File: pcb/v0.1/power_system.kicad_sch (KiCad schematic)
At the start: 6 parts, among them J12 USB_C_Receptacle_USB2.0

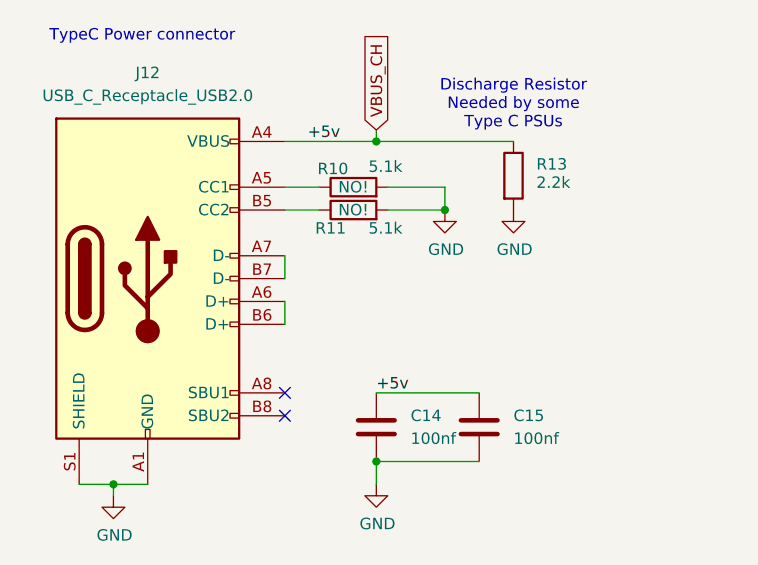
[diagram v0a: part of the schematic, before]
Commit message: More work on the sound system
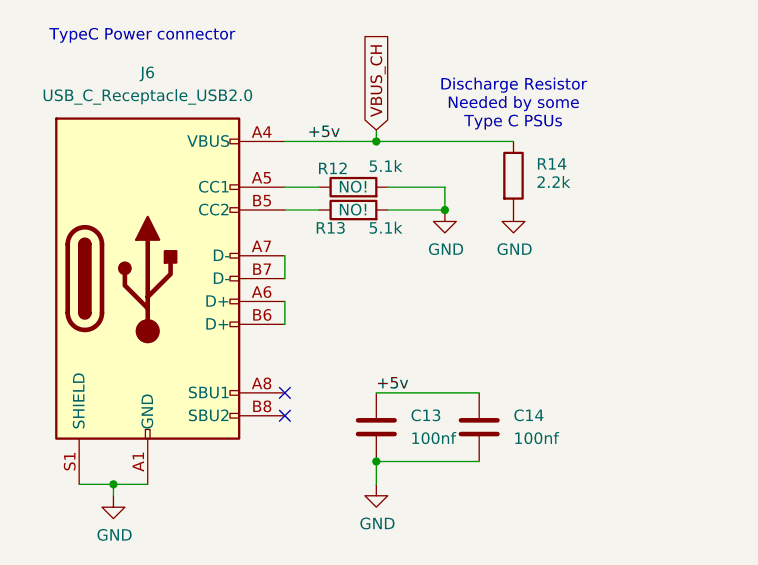
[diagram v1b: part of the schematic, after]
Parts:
- renumbered C14 to C13, C15 to C14, J12 to J6, R10 to R12, R11 to R13, R13 to R14
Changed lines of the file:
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@@
 		(dnp no)
 		(fields_autoplaced yes)
-		(property "Reference" "C15"
+		(property "Reference" "C14"
 			(at 106.68 87.63 0)
 			(show_name no)
@@
 			(project "mainboard"
 				(path "/5b8aa782-5c3d-43e7-a869-3bd000015f52/6125d0a9-a152-4232-a300-1c14841893d5"
-					(reference "C15")
+					(reference "C14")
 					(unit 1)
 				)
@@
 		(in_pos_files yes)
 		(dnp no)
-		(property "Reference" "#PWR020"
+		(property "Reference" "#PWR030"
 			(at 62.23 102.87 0)
 			(hide yes)
@@
 			(project "mainboard"
 				(path "/5b8aa782-5c3d-43e7-a869-3bd000015f52/6125d0a9-a152-4232-a300-1c14841893d5"
-					(reference "#PWR020")
+					(reference "#PWR030")
 					(unit 1)
 				)
@@
 		(in_pos_files yes)
 		(dnp no)
-		(property "Reference" "R11"
+		(property "Reference" "R13"
 			(at 86.36 66.802 90)
 			(show_name no)
@@
 			(project "mainboard"
 				(path "/5b8aa782-5c3d-43e7-a869-3bd000015f52/6125d0a9-a152-4232-a300-1c14841893d5"
-					(reference "R11")
+					(reference "R13")
 					(unit 1)
 				)
@@
 		(in_pos_files yes)
 		(dnp no)
-		(property "Reference" "#PWR034"
+		(property "Reference" "#PWR033"
 			(at 106.68 71.12 0)
 			(hide yes)
@@
 			(project "mainboard"
 				(path "/5b8aa782-5c3d-43e7-a869-3bd000015f52/6125d0a9-a152-4232-a300-1c14841893d5"
-					(reference "#PWR034")
+					(reference "#PWR033")
 					(unit 1)
 				)
@@
 		(dnp no)
 		(fields_autoplaced yes)
-		(property "Reference" "J12"
+		(property "Reference" "J6"
 			(at 66.04 49.53 0)
 			(show_name no)
@@
 			(project "mainboard"
 				(path "/5b8aa782-5c3d-43e7-a869-3bd000015f52/6125d0a9-a152-4232-a300-1c14841893d5"
-					(reference "J12")
+					(reference "J6")
 					(unit 1)
 				)
@@
 		(in_pos_files yes)
 		(dnp no)
-		(property "Reference" "R10"
+		(property "Reference" "R12"
 			(at 86.614 60.198 90)
 			(show_name no)
@@
 			(project "mainboard"
 				(path "/5b8aa782-5c3d-43e7-a869-3bd000015f52/6125d0a9-a152-4232-a300-1c14841893d5"
-					(reference "R10")
+					(reference "R12")
 					(unit 1)
 				)
@@
 		(in_pos_files yes)
 		(dnp no)
-		(property "Reference" "#PWR021"
+		(property "Reference" "#PWR031"
 			(at 91.44 101.6 0)
 			(hide yes)
@@
 			(project "mainboard"
 				(path "/5b8aa782-5c3d-43e7-a869-3bd000015f52/6125d0a9-a152-4232-a300-1c14841893d5"
-					(reference "#PWR021")
+					(reference "#PWR031")
 					(unit 1)
 				)
@@
 		(dnp no)
 		(fields_autoplaced yes)
-		(property "Reference" "C14"
+		(property "Reference" "C13"
 			(at 95.25 87.63 0)
 			(show_name no)
@@
 			(project "mainboard"
 				(path "/5b8aa782-5c3d-43e7-a869-3bd000015f52/6125d0a9-a152-4232-a300-1c14841893d5"
-					(reference "C14")
+					(reference "C13")
 					(unit 1)
 				)
@@
 		(in_pos_files yes)
 		(dnp no)
-		(property "Reference" "#PWR033"
+		(property "Reference" "#PWR032"
 			(at 99.06 71.12 0)
 			(hide yes)
@@
 			(project "mainboard"
 				(path "/5b8aa782-5c3d-43e7-a869-3bd000015f52/6125d0a9-a152-4232-a300-1c14841893d5"
-					(reference "#PWR033")
+					(reference "#PWR032")
 					(unit 1)
 				)
@@
 		(in_pos_files yes)
 		(dnp no)
-		(property "Reference" "R13"
+		(property "Reference" "R14"
 			(at 109.22 59.69 0)
 			(show_name no)
@@
 			(project "mainboard"
 				(path "/5b8aa782-5c3d-43e7-a869-3bd000015f52/6125d0a9-a152-4232-a300-1c14841893d5"
-					(reference "R13")
+					(reference "R14")
 					(unit 1)
 				)

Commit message: Dac finished
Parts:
- renumbered C13 to C22, C14 to C23, R12 to R14, R13 to R15, R14 to R16
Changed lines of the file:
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@@
 		(dnp no)
 		(fields_autoplaced yes)
-		(property "Reference" "C14"
+		(property "Reference" "C23"
 			(at 106.68 87.63 0)
 			(show_name no)
@@
 			(project "mainboard"
 				(path "/5b8aa782-5c3d-43e7-a869-3bd000015f52/6125d0a9-a152-4232-a300-1c14841893d5"
-					(reference "C14")
+					(reference "C23")
 					(unit 1)
 				)
@@
 		(in_pos_files yes)
 		(dnp no)
-		(property "Reference" "#PWR030"
+		(property "Reference" "#PWR037"
 			(at 62.23 102.87 0)
 			(hide yes)
@@
 			(project "mainboard"
 				(path "/5b8aa782-5c3d-43e7-a869-3bd000015f52/6125d0a9-a152-4232-a300-1c14841893d5"
-					(reference "#PWR030")
+					(reference "#PWR037")
 					(unit 1)
 				)
@@
 		(in_pos_files yes)
 		(dnp no)
-		(property "Reference" "R13"
+		(property "Reference" "R15"
 			(at 86.36 66.802 90)
 			(show_name no)
@@
 			(project "mainboard"
 				(path "/5b8aa782-5c3d-43e7-a869-3bd000015f52/6125d0a9-a152-4232-a300-1c14841893d5"
-					(reference "R13")
+					(reference "R15")
 					(unit 1)
 				)
@@
 		(in_pos_files yes)
 		(dnp no)
-		(property "Reference" "#PWR033"
+		(property "Reference" "#PWR040"
 			(at 106.68 71.12 0)
 			(hide yes)
@@
 			(project "mainboard"
 				(path "/5b8aa782-5c3d-43e7-a869-3bd000015f52/6125d0a9-a152-4232-a300-1c14841893d5"
-					(reference "#PWR033")
+					(reference "#PWR040")
 					(unit 1)
 				)
@@
 		(in_pos_files yes)
 		(dnp no)
-		(property "Reference" "R12"
+		(property "Reference" "R14"
 			(at 86.614 60.198 90)
 			(show_name no)
@@
 			(project "mainboard"
 				(path "/5b8aa782-5c3d-43e7-a869-3bd000015f52/6125d0a9-a152-4232-a300-1c14841893d5"
-					(reference "R12")
+					(reference "R14")
 					(unit 1)
 				)
@@
 		(in_pos_files yes)
 		(dnp no)
-		(property "Reference" "#PWR031"
+		(property "Reference" "#PWR038"
 			(at 91.44 101.6 0)
 			(hide yes)
@@
 			(project "mainboard"
 				(path "/5b8aa782-5c3d-43e7-a869-3bd000015f52/6125d0a9-a152-4232-a300-1c14841893d5"
-					(reference "#PWR031")
+					(reference "#PWR038")
 					(unit 1)
 				)
@@
 		(dnp no)
 		(fields_autoplaced yes)
-		(property "Reference" "C13"
+		(property "Reference" "C22"
 			(at 95.25 87.63 0)
 			(show_name no)
@@
 			(project "mainboard"
 				(path "/5b8aa782-5c3d-43e7-a869-3bd000015f52/6125d0a9-a152-4232-a300-1c14841893d5"
-					(reference "C13")
+					(reference "C22")
 					(unit 1)
 				)
@@
 		(in_pos_files yes)
 		(dnp no)
-		(property "Reference" "#PWR032"
+		(property "Reference" "#PWR039"
 			(at 99.06 71.12 0)
 			(hide yes)
@@
 			(project "mainboard"
 				(path "/5b8aa782-5c3d-43e7-a869-3bd000015f52/6125d0a9-a152-4232-a300-1c14841893d5"
-					(reference "#PWR032")
+					(reference "#PWR039")
 					(unit 1)
 				)
@@
 		(in_pos_files yes)
 		(dnp no)
-		(property "Reference" "R14"
+		(property "Reference" "R16"
 			(at 109.22 59.69 0)
 			(show_name no)
@@
 			(project "mainboard"
 				(path "/5b8aa782-5c3d-43e7-a869-3bd000015f52/6125d0a9-a152-4232-a300-1c14841893d5"
-					(reference "R14")
+					(reference "R16")
 					(unit 1)
 				)

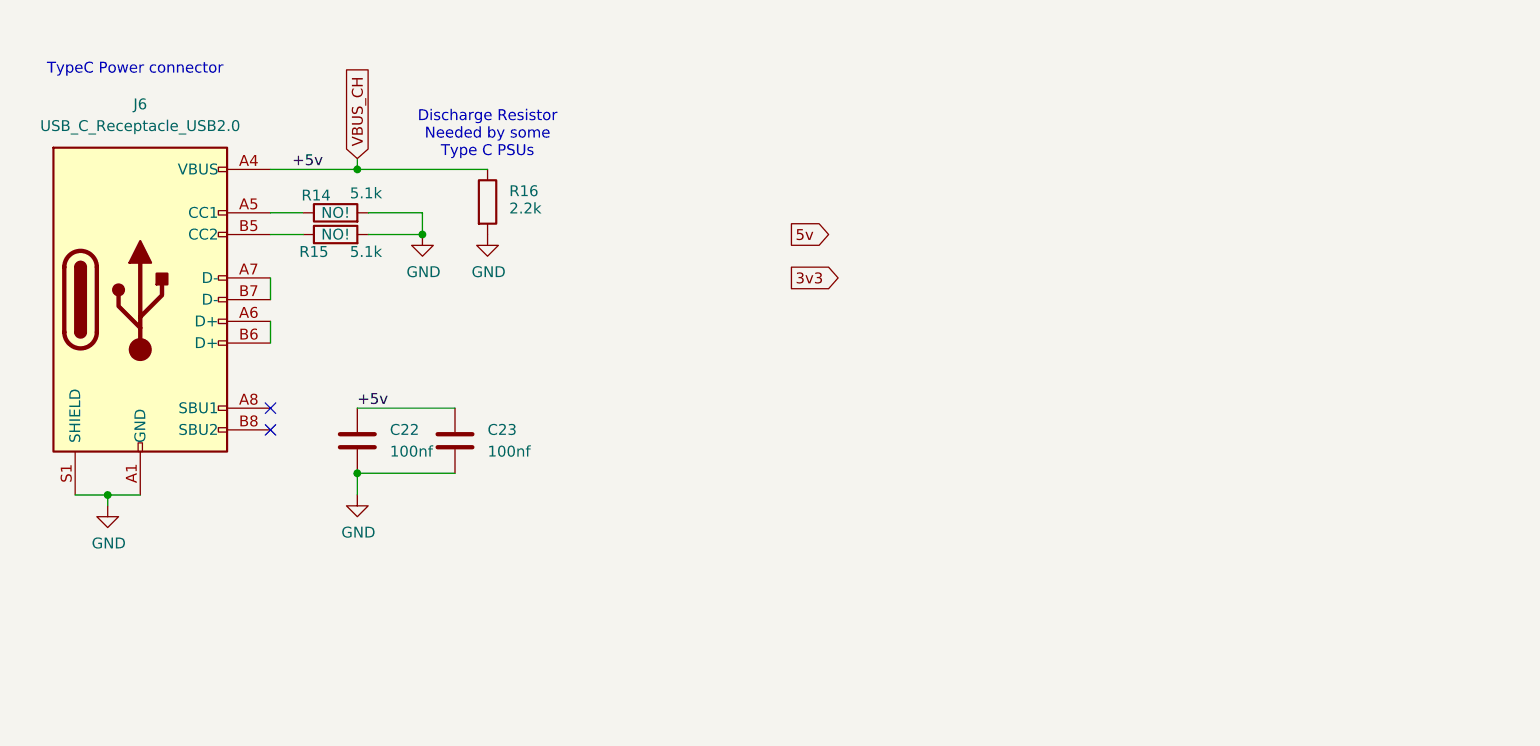
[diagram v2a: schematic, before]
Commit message: Add 3v3 regulator + reshuffle some connections.
Regulator ported over directly from PDB. I've also had to change around
some of the connections between modules to keep up with requirements.
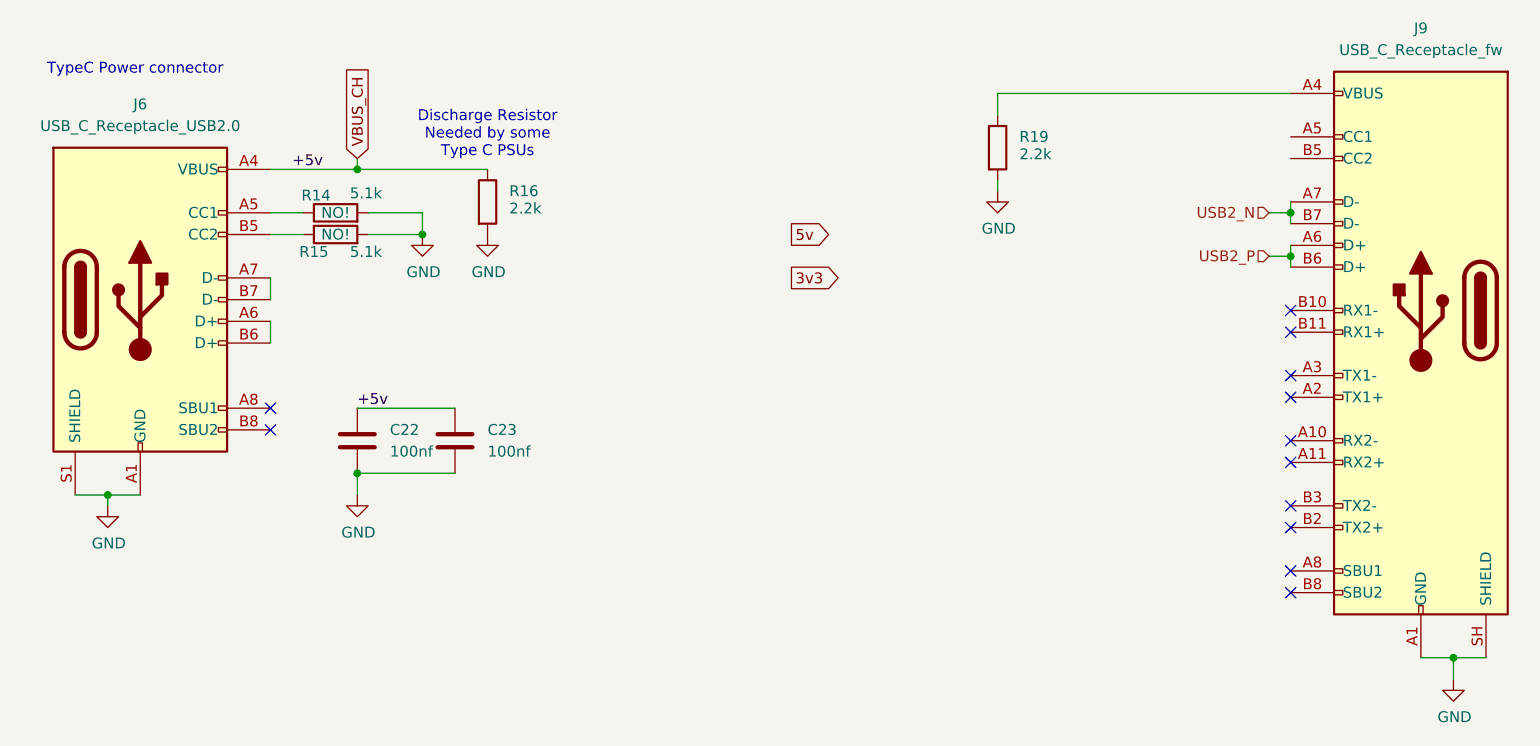
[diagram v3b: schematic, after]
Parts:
- added J9: USB_C_Receptacle_fw, symbol TH-1-CC:USB_C_Receptacle_fw
- added R19: 2.2k, Resistor_SMD:R_0603_1608Metric, symbol TH-1-CC:R_2.2k
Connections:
- net GND: now also J9.A1 (GND), J9.A12 (GND), J9.B1 (GND), J9.B12 (GND), J9.SH (SHIELD), R19.2
- new net: J9.A4 (VBUS), J9.A9 (VBUS), J9.B4 (VBUS), J9.B9 (VBUS), R19.1
- new net USB2_N: J9.A7 (D-), J9.B7 (D-)
- new net USB2_P: J9.A6 (D+), J9.B6 (D+)
- no-connect marks 2 -> 12
